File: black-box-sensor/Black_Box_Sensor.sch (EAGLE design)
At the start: 39 parts, among them J1 104031-0811, J2 UX60-MB-5S8, J3 B4B-PH-SM4-TBT(LF)(SN), U1 ADXL375, U2 ADXL375, U3 ATMEGA32U4-AU, U4 FXAS21002CQR1, U5 MIC5504-3.3YM5-TR, U6 NL27WZ32USG, U7 MAX7375AXR805T, U8 AD8426ACPZ-WP

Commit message: black box sensor changes
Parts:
- added ISP1: AVRISP-6, adafruit:AVRISP-6
- LED1: value (none) -> GREEN
- LED2: value (none) -> PINK
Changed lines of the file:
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@@
 <part name="SUPPLY15" library="SparkFun-PowerSymbols" deviceset="3.3V" device=""/>
 <part name="GND22" library="SparkFun-PowerSymbols" deviceset="GND" device=""/>
-<part name="LED1" library="led" library_urn="urn:adsk.eagle:library:259" deviceset="LED" device="CHIP-LED0805" package3d_urn="urn:adsk.eagle:package:15818/2">
+<part name="LED1" library="led" library_urn="urn:adsk.eagle:library:259" deviceset="LED" device="CHIP-LED0805" package3d_urn="urn:adsk.eagle:package:15818/2" value="GREEN">
 <attribute name="DJKPN" value="3372-0805YGBD008S01TR-ND"/>
 </part>
 <part name="SUPPLY16" library="SparkFun-PowerSymbols" deviceset="3.3V" device=""/>
-<part name="LED2" library="led" library_urn="urn:adsk.eagle:library:259" deviceset="LED" device="KA-3528ASYC" package3d_urn="urn:adsk.eagle:package:15831/1">
+<part name="LED2" library="led" library_urn="urn:adsk.eagle:library:259" deviceset="LED" device="KA-3528ASYC" package3d_urn="urn:adsk.eagle:package:15831/1" value="PINK">
 <attribute name="DJKPN" value="754-1534-1-ND"/>
 </part>
@@
 <part name="SUPPLY17" library="RoboJackets-Supplies" deviceset="VBATT" device=""/>
 <part name="GND25" library="SparkFun-PowerSymbols" deviceset="GND" device=""/>
+<part name="ISP1" library="adafruit" library_urn="urn:adsk.eagle:library:420" deviceset="AVRISP" device="-6" package3d_urn="urn:adsk.eagle:package:6240744/1"/>
+<part name="SUPPLY18" library="SparkFun-PowerSymbols" deviceset="3.3V" device=""/>
+<part name="GND26" library="SparkFun-PowerSymbols" deviceset="GND" device=""/>
 </parts>
 <sheets>
@@
 <instance part="GND25" gate="1" x="132.08" y="101.6" smashed="yes">
 <attribute name="VALUE" x="132.08" y="101.346" size="1.778" layer="96" align="top-center"/>
+</instance>
+<instance part="ISP1" gate="G$1" x="-48.26" y="5.08" smashed="yes">
+<attribute name="NAME" x="-50.8" y="-2.54" size="1.778" layer="95"/>
+</instance>
+<instance part="SUPPLY18" gate="G$1" x="-27.94" y="7.62" smashed="yes">
+<attribute name="VALUE" x="-27.94" y="10.414" size="1.778" layer="96" align="bottom-center"/>
+</instance>
+<instance part="GND26" gate="1" x="203.2" y="-60.96" smashed="yes">
+<attribute name="VALUE" x="203.2" y="-61.214" size="1.778" layer="96" align="top-center"/>
 </instance>
 </instances>
@@
 <wire x1="203.2" y1="-55.88" x2="193.04" y2="-55.88" width="0.1524" layer="91"/>
 <wire x1="193.04" y1="-55.88" x2="193.04" y2="-68.58" width="0.1524" layer="91"/>
-<wire x1="193.04" y1="-68.58" x2="243.84" y2="-68.58" width="0.1524" layer="91"/>
-<wire x1="243.84" y1="-68.58" x2="243.84" y2="-50.8" width="0.1524" layer="91"/>
+</segment>
+<segment>
+<pinref part="U8" gate="G$1" pin="REFA"/>
+<wire x1="233.68" y1="-25.4" x2="238.76" y2="-25.4" width="0.1524" layer="91"/>
+<label x="238.76" y="-25.4" size="1.27" layer="95" xref="yes"/>
+</segment>
+<segment>
 <pinref part="U8" gate="G$1" pin="OUTB"/>
 <wire x1="243.84" y1="-50.8" x2="233.68" y2="-50.8" width="0.1524" layer="91"/>
 <label x="243.84" y="-50.8" size="1.27" layer="95" xref="yes"/>
 </segment>
-<segment>
-<pinref part="U8" gate="G$1" pin="REFA"/>
-<wire x1="233.68" y1="-25.4" x2="238.76" y2="-25.4" width="0.1524" layer="91"/>
-<label x="238.76" y="-25.4" size="1.27" layer="95" xref="yes"/>
-</segment>
-</net>
+</net>

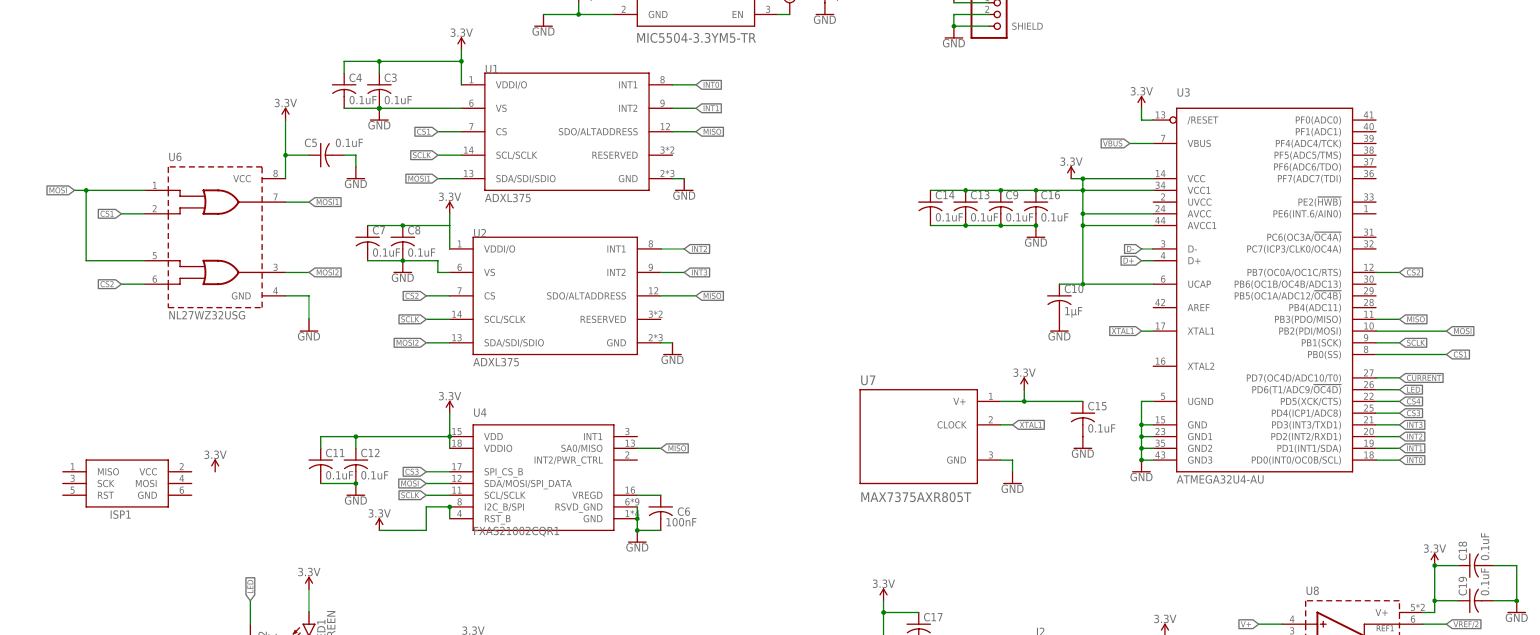
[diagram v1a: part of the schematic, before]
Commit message: Adding level shifter to run MCU at 5V
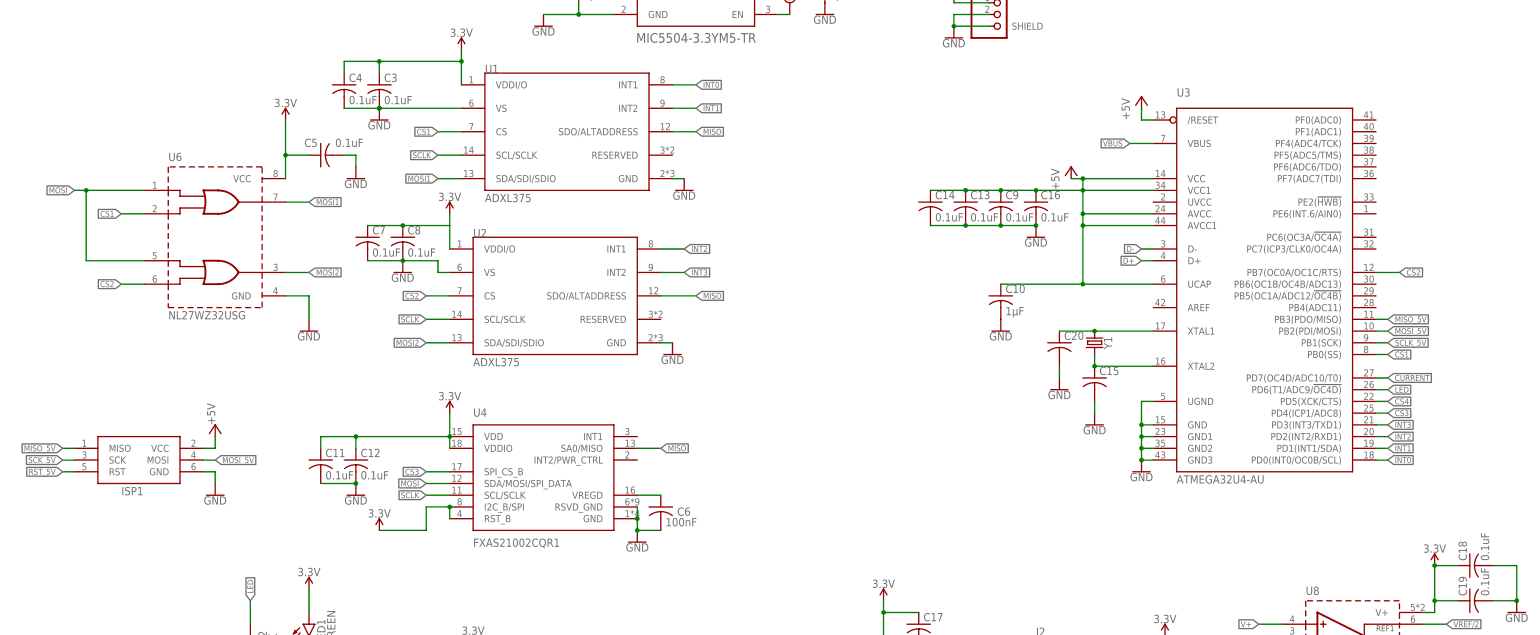
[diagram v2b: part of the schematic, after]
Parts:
- removed U7: MAX7375AXR805T, BBS_Library:MAX7375AXR805T
- added C20: (no value), rcl:C-USC0603
- added Y1: (no value), SparkFun-Clocks:CRYSTALSMD-3.2X2.5
- C15: value 0.1uF -> (none); DKPN CGA3E2X7R1E104K080AA -> (none)
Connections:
- new net +5V: C10.1, C13.1, C14.1, C16.1, C9.1, ISP1.VCC, U3./RESET, U3.AVCC, U3.AVCC1, U3.UCAP, U3.VCC, U3.VCC1
- new net MISO_5V: ISP1.MISO, U3.PB3(PDO/MISO)
- new net MOSI_5V: ISP1.MOSI, U3.PB2(PDI/MOSI)
- new net N$7: C15.1, U3.XTAL2, Y1.2
- new net RST_5V: ISP1.RST
- new net SCK_5V: ISP1.SCK
- new net SCLK_5V: U3.PB1(SCK)
- net 3.3V: no longer C10.1, C13.1, C14.1, C15.1, C16.1, C9.1, U3./RESET, U3.AVCC, U3.AVCC1, U3.UCAP, U3.VCC, U3.VCC1, U7.V+
- net GND: now also C20.2, ISP1.GND; no longer U7.GND
- net MISO: no longer U3.PB3(PDO/MISO)
- net MOSI: no longer U3.PB2(PDI/MOSI)
- net SCLK: no longer U3.PB1(SCK)
- net XTAL1: now also C20.1, Y1.1; no longer U7.CLOCK
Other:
- moved on the sheet: C10, C15, ISP1

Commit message: add level shifter to bbs lib
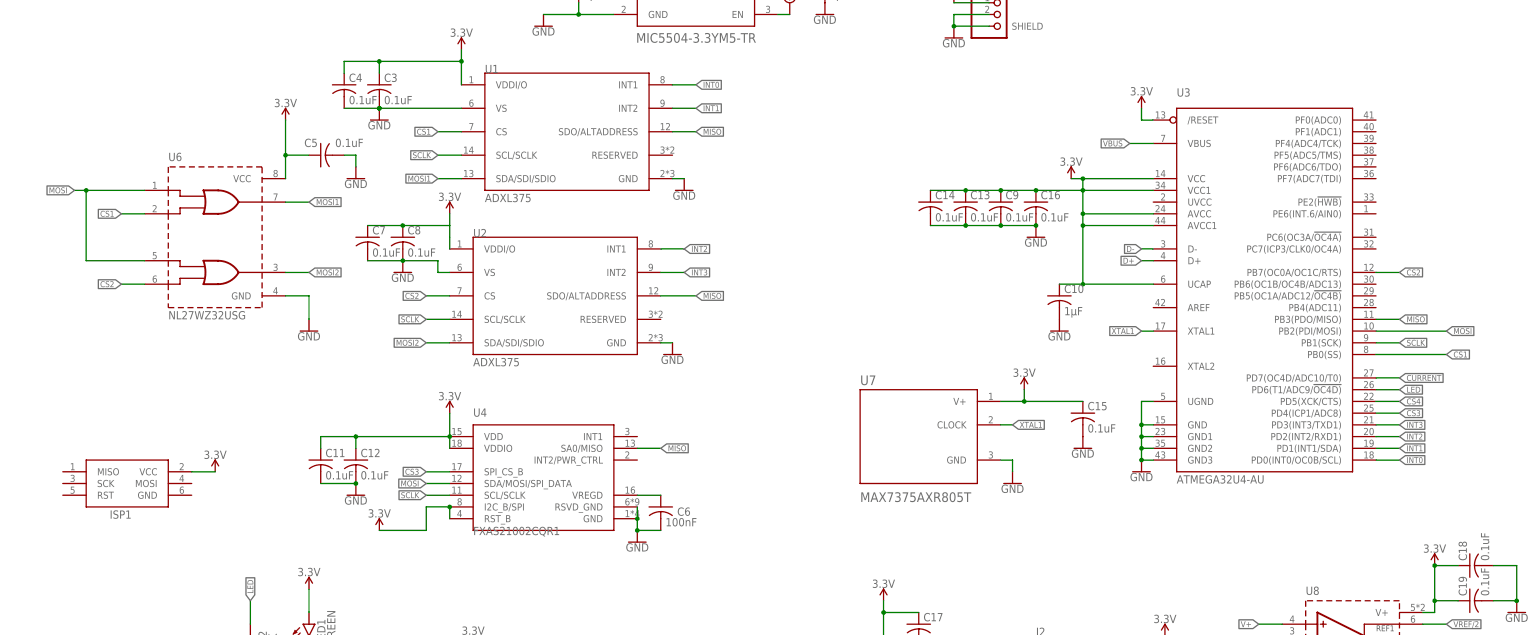
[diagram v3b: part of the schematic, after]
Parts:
- removed C20: (no value), rcl:C-USC0603
- removed Y1: (no value), SparkFun-Clocks:CRYSTALSMD-3.2X2.5
- added U7: MAX7375AXR805T, BBS_Library:MAX7375AXR805T
- C15: value (none) -> 0.1uF; DKPN (none) -> CGA3E2X7R1E104K080AA
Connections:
- removed net +5V: C10.1, C13.1, C14.1, C16.1, C9.1, ISP1.VCC, U3./RESET, U3.AVCC, U3.AVCC1, U3.UCAP, U3.VCC, U3.VCC1
- removed net MISO_5V: ISP1.MISO, U3.PB3(PDO/MISO)
- removed net MOSI_5V: ISP1.MOSI, U3.PB2(PDI/MOSI)
- removed net N$7: C15.1, U3.XTAL2, Y1.2
- removed net RST_5V: ISP1.RST
- removed net SCK_5V: ISP1.SCK
- removed net SCLK_5V: U3.PB1(SCK)
- net 3.3V: now also C10.1, C13.1, C14.1, C15.1, C16.1, C9.1, ISP1.VCC, U3./RESET, U3.AVCC, U3.AVCC1, U3.UCAP, U3.VCC, U3.VCC1, U7.V+
- net GND: now also U7.GND; no longer C20.2, ISP1.GND
- net MISO: now also U3.PB3(PDO/MISO)
- net MOSI: now also U3.PB2(PDI/MOSI)
- net SCLK: now also U3.PB1(SCK)
- net XTAL1: now also U7.CLOCK; no longer C20.1, Y1.1
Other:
- moved on the sheet: C10, C15, ISP1

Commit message: Revert "add level shifter to bbs lib"
This reverts commit 934bd0793bafe6a139599fb7599099a5d3743223.
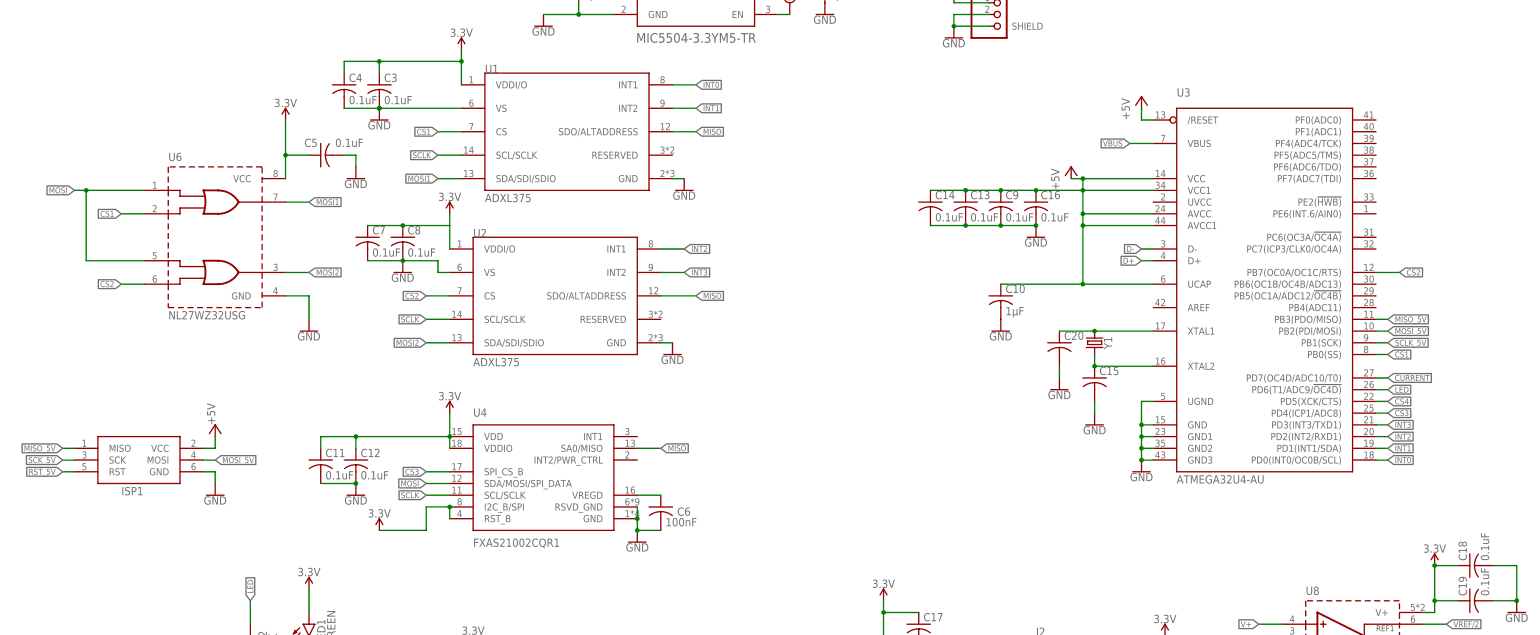
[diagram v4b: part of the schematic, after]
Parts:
- removed U7: MAX7375AXR805T, BBS_Library:MAX7375AXR805T
- added C20: (no value), rcl:C-USC0603
- added Y1: (no value), SparkFun-Clocks:CRYSTALSMD-3.2X2.5
- C15: value 0.1uF -> (none); DKPN CGA3E2X7R1E104K080AA -> (none)
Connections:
- new net +5V: C10.1, C13.1, C14.1, C16.1, C9.1, ISP1.VCC, U3./RESET, U3.AVCC, U3.AVCC1, U3.UCAP, U3.VCC, U3.VCC1
- new net MISO_5V: ISP1.MISO, U3.PB3(PDO/MISO)
- new net MOSI_5V: ISP1.MOSI, U3.PB2(PDI/MOSI)
- new net N$7: C15.1, U3.XTAL2, Y1.2
- new net RST_5V: ISP1.RST
- new net SCK_5V: ISP1.SCK
- new net SCLK_5V: U3.PB1(SCK)
- net 3.3V: no longer C10.1, C13.1, C14.1, C15.1, C16.1, C9.1, ISP1.VCC, U3./RESET, U3.AVCC, U3.AVCC1, U3.UCAP, U3.VCC, U3.VCC1, U7.V+
- net GND: now also C20.2, ISP1.GND; no longer U7.GND
- net MISO: no longer U3.PB3(PDO/MISO)
- net MOSI: no longer U3.PB2(PDI/MOSI)
- net SCLK: no longer U3.PB1(SCK)
- net XTAL1: now also C20.1, Y1.1; no longer U7.CLOCK
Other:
- moved on the sheet: C10, C15, ISP1

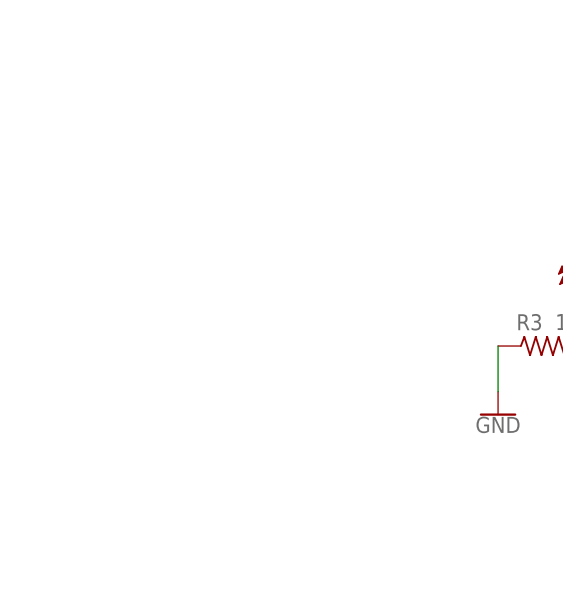
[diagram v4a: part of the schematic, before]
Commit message: add level shifter to schematic
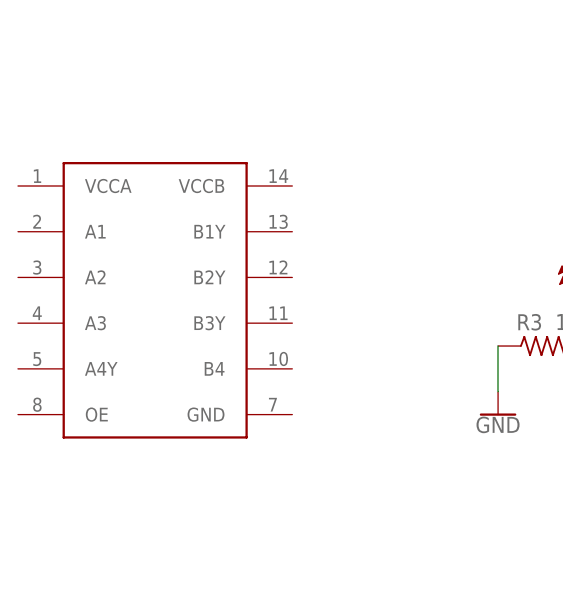
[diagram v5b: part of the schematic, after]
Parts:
- added U$1: TXU0304, BBS_Library:TXU0304
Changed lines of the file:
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@@
 <part name="P+3" library="supply1" library_urn="urn:adsk.eagle:library:371" deviceset="+5V" device=""/>
 <part name="GND27" library="SparkFun-PowerSymbols" deviceset="GND" device=""/>
+<part name="U$1" library="BBS_Library" deviceset="TXU0304" device=""/>
 </parts>
 <sheets>
@@
 <attribute name="VALUE" x="-27.94" y="2.286" size="1.778" layer="96" align="top-center"/>
 </instance>
+<instance part="U$1" gate="G$1" x="-68.58" y="-33.02" smashed="yes"/>
 </instances>
 <busses>
